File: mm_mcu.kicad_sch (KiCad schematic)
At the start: 18 parts, among them J1 Conn_ARM_JTAG_SWD_10, U1 STM32F030C8Tx

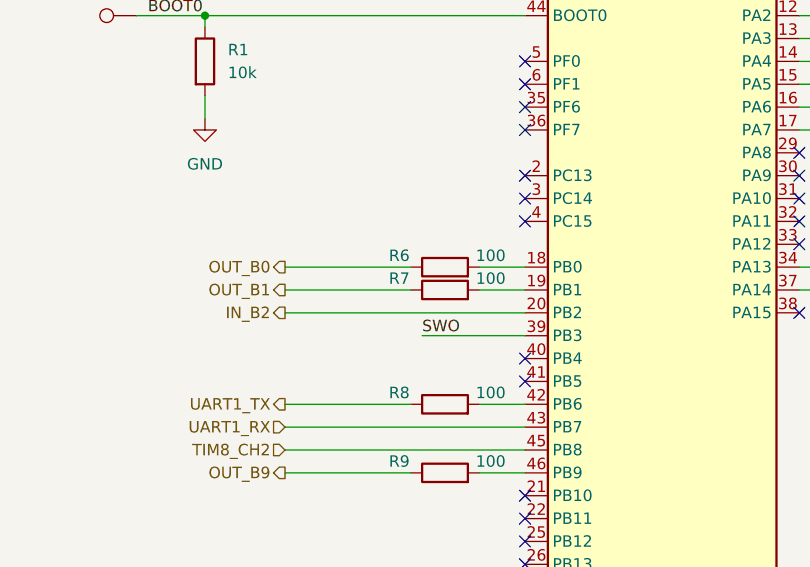
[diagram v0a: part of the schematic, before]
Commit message: ended PCB + added reverse voltage protection
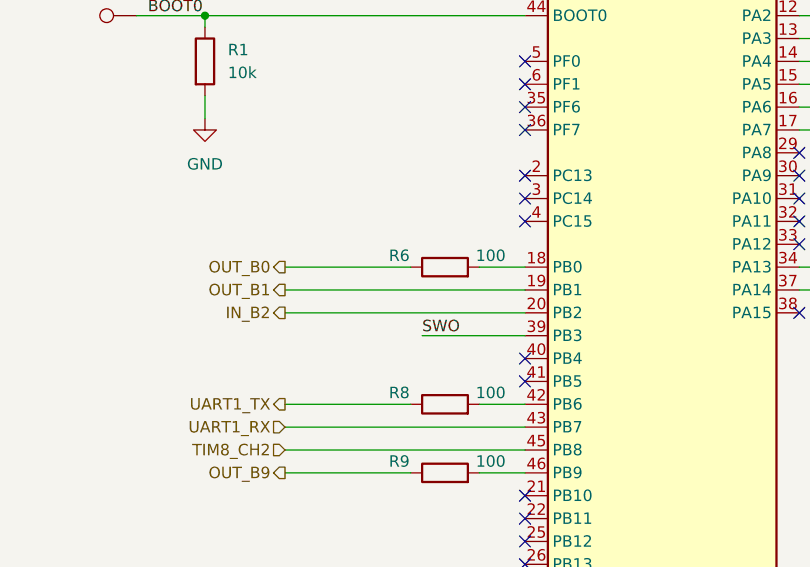
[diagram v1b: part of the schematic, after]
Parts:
- removed R7: 100, Resistor_SMD:R_0603_1608Metric, symbol Device:R
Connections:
- net OUT_B1: now also U1.19 (PB1)
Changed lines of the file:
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@@
-    (stroke (width 0) (type default))
-  )
-  (wire (pts (xy 97.79 77.47) (xy 111.76 77.47))
     (stroke (width 0) (type default))
   )
@@
     (stroke (width 0) (type default))
   )
-  (wire (pts (xy 119.38 77.47) (xy 124.46 77.47))
+  (wire (pts (xy 97.79 77.47) (xy 124.46 77.47))
     (stroke (width 0) (type default))
   )
@@
         )
       )
-    )
-  )
-  (symbol (lib_id "Device:R") (at 115.57 77.47 90) (unit 1)
-    (in_bom yes) (on_board yes) (dnp no)
-    (property "Reference" "R7" (at 110.49 76.2 90)
-      (effects (font (size 1.27 1.27)))
-    )
-    (property "Value" "100" (at 120.65 76.2 90)
-      (effects (font (size 1.27 1.27)))
-    )
-    (property "Footprint" "Resistor_SMD:R_0603_1608Metric" (at 115.57 79.248 90)
-      (effects (font (size 1.27 1.27)) hide)
-    )
-    (property "Datasheet" "~" (at 115.57 77.47 0)
-      (effects (font (size 1.27 1.27)) hide)
-    )
-    (pin "1")
-    (pin "2")
-    (instances
-      (project "minimouse"
-        (path "/d8fa4cba-2469-4231-847f-065b6b829f44/b5d7e952-00af-4b6f-924a-ee43c62726d2"
-          (reference "R7") (unit 1)
-        )
-      )
